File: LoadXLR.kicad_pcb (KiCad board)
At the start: 2 copper layers, 70 x 90 mm, 23 parts, among them J1 NC3MAH, J2 NC3FAH2, J3 NC3MAH, J4 NC3FAH2, SW1 SW_DIP_x10

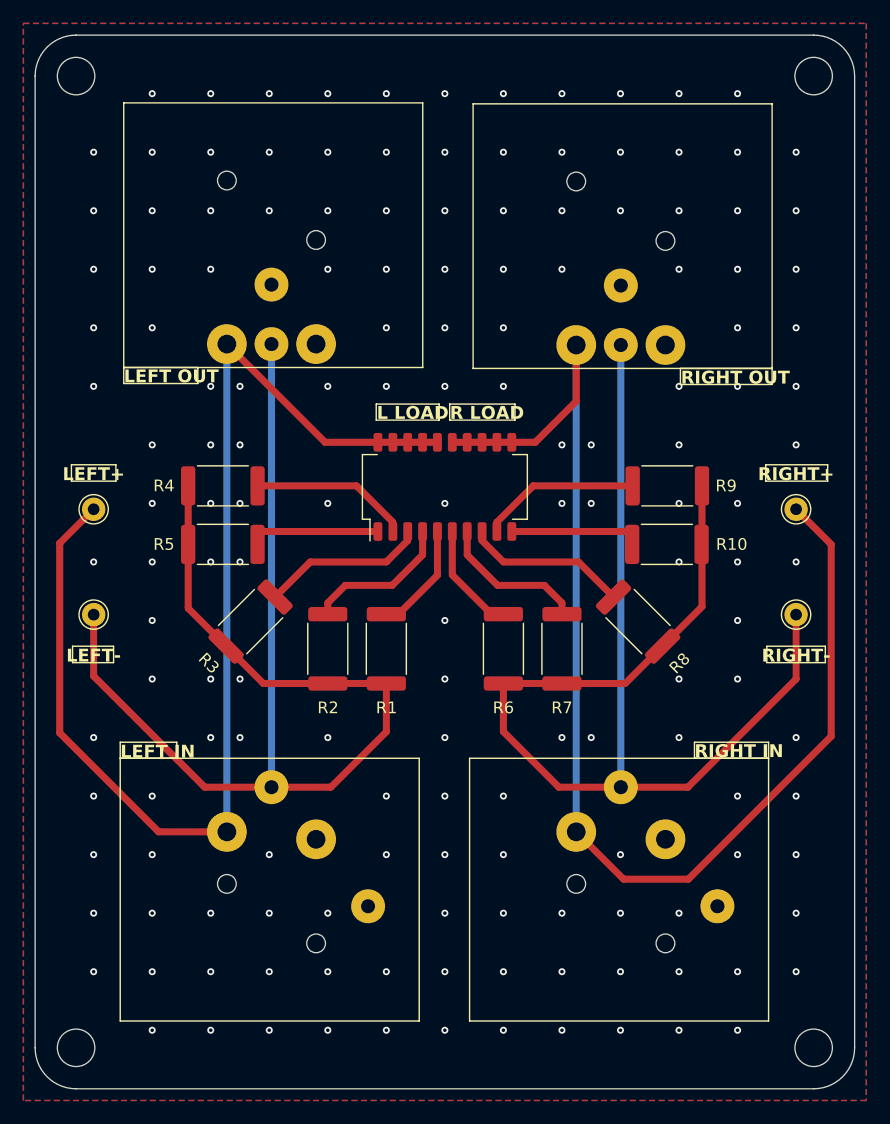
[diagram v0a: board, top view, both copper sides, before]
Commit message: Board layout
Updated the board layout.
Added a picture of the board render.
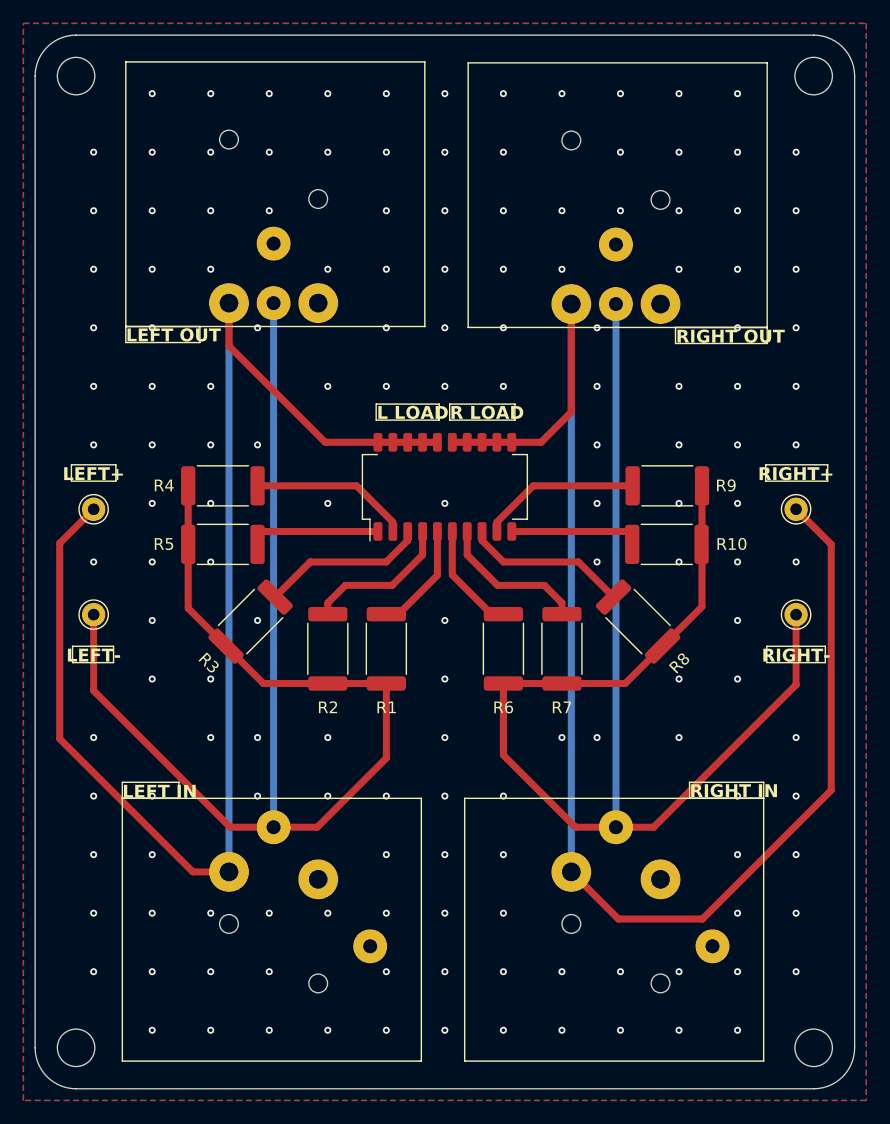
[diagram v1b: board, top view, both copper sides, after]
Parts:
- added G***: LOGO, Logos:LoadXLR, B.Cu at (132.9, 104.9)
- moved J3 3.53 mm to (153.4, 63.0)
- moved J1 3.50 mm to (124.2, 62.9)
- moved J4 3.45 mm to (153.4, 112.1)
- moved J2 3.42 mm to (124.2, 112.1)
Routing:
- net /R+: track 107.6 -> 122.6 mm
- net /L+: track 101.2 -> 113.4 mm
- net /L-: track 108.2 -> 120.0 mm
- net /R-: track 108.2 -> 119.4 mm
- net GND: vias 157 -> 155
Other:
- board text added: "LOAD XLR"
- board text added: "PD 07/25"
- board text added: "REV A"
- board text added: "V1.0"
